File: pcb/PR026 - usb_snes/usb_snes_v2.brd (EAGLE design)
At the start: 34.3 x 22.9 mm, 16 parts, among them IC1 AVR-MEGA8, IC2 SNES

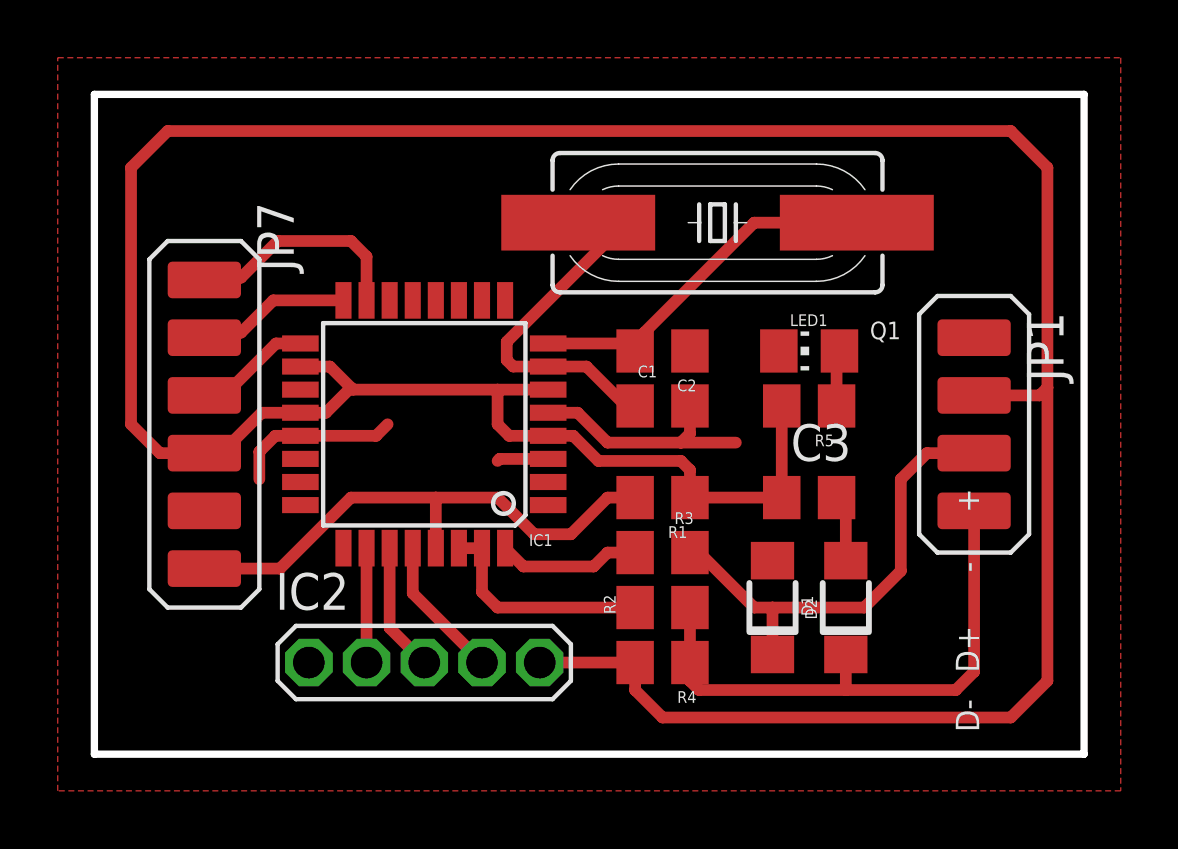
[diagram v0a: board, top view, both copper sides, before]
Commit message: 
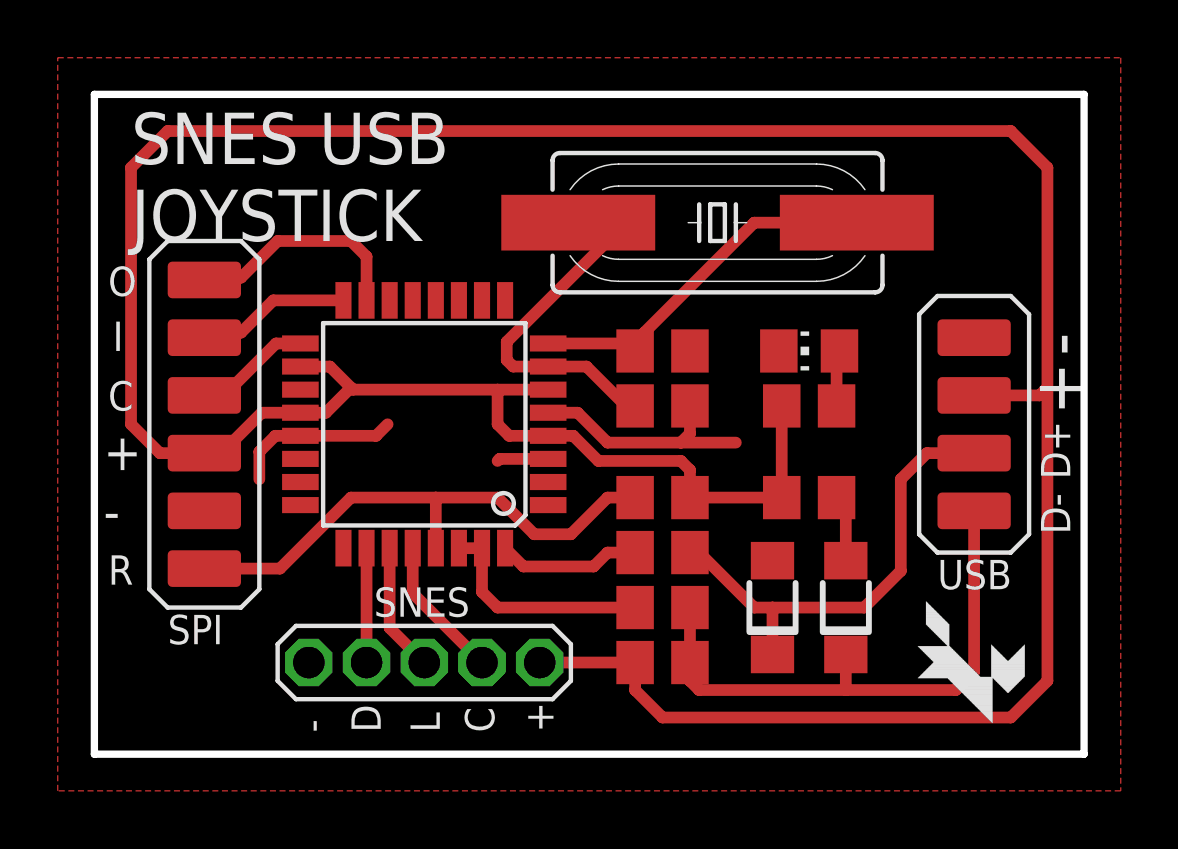
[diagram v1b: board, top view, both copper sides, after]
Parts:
- added U$1: (no value), usb_snes:FOX-1
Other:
- board text added: "C"
- board text added: "D"
- board text added: "I"
- board text added: "L"
- board text added: "O"
- board text added: "R"
- board text added: "SNES"
- board text added: "SNES USB JOYSTICK"
- board text added: "SPI"
- board text added: "USB"

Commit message: 
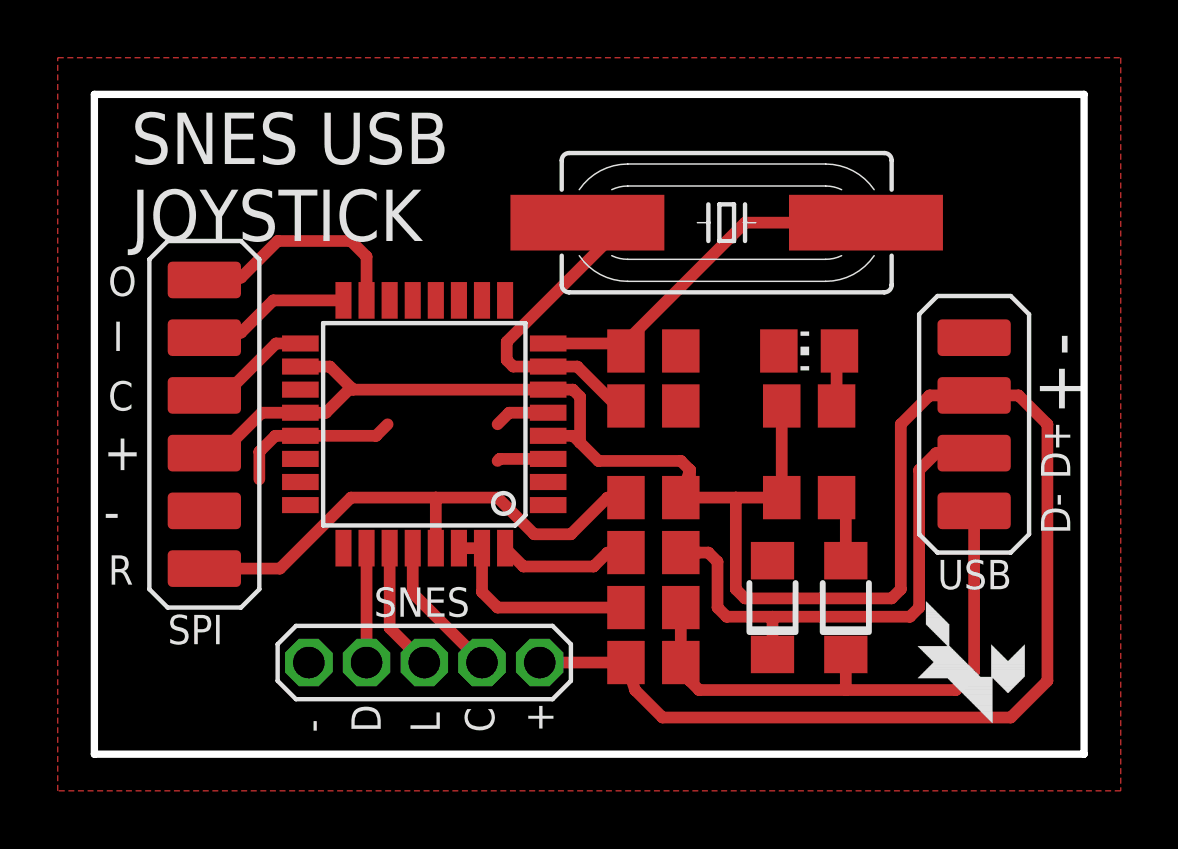
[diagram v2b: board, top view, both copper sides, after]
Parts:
- moved C1 0.32 mm to (19.4, 12.1)
- moved C2 0.32 mm to (19.4, 14.0)
- moved Q1 0.32 mm to (21.9, 18.4)
- moved R1 0.32 mm to (19.4, 8.89)
- moved R2 0.32 mm to (19.4, 5.08)
- moved R3 0.32 mm to (19.4, 6.99)
- moved R4 0.32 mm to (19.4, 3.17)
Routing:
- net +5V: track 115.3 -> 80.6 mm
- net GND: track 18.9 -> 12.5 mm
- net D+: track 16.3 -> 19.1 mm
- net N$3: track 12.4 -> 11.7 mm
- net N$2: track 12.8 -> 13.4 mm
